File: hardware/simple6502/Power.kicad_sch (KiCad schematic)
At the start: 11 parts, among them J6 AUX 5VDC, U5 74HCT00, U6 74LS30

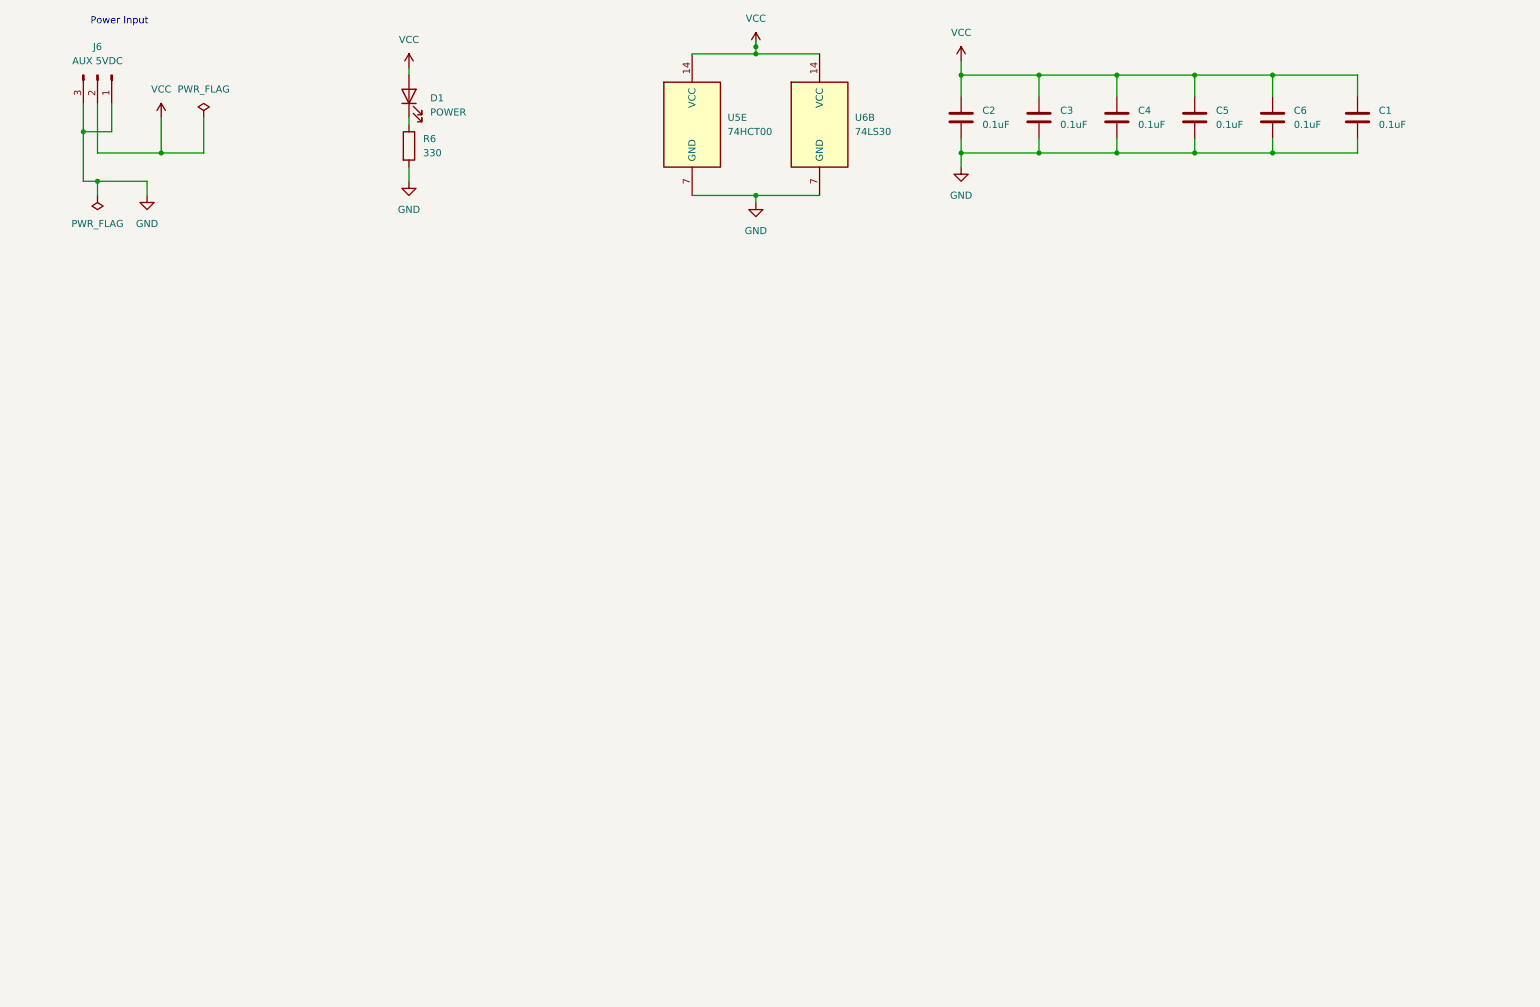
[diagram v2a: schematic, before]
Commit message: Squashed commit of the following:
commit 7c3efda86e123a872d37b7a0967bfebff1f0e87c
Author: Mariano Luna <marianolu@gmail.com>
Date:   Wed Jun 26 21:29:25 2024 -0500

    added license to the read me

commit 04e24ff3751ecfd7aa1644195e6f678569023e69
Author: Mariano Luna <marianolu@gmail.com>
Date:   Wed Jun 26 21:19:54 2024 -0500

    typo fix for {\textunderscore}

commit 2b909ce419fda75b2b3b71af0dca9a0f271ced5f
Author: Mariano Luna <marianolu@gmail.com>
Date:   Wed Jun 26 21:10:17 2024 -0500

    updated ReadME and memory map in the schematic

commit 245ee8cf40a99742bf88408506d7aad409daa5ea
Author: Mariano Luna <marianolu@gmail.com>
Date:   Wed Jun 26 20:32:31 2024 -0500

    minor slikscreen additions

commit ba4f0f790206ee10e8f2da3f956f1fdfcce2d174
Author: Mariano Luna <marianolu@gmail.com>
Date:   Wed Jun 26 20:23:09 2024 -0500

    new PCB pics

commit 7135a14f7811bac113619ea70f1b15383090e088
Author: Mariano Luna <marianolu@gmail.com>
Date:   Wed Jun 26 20:16:23 2024 -0500

    minor silkscreen and trace tidy up

commit cb74d108b563011aa3ae8e77489211a7feb419d9
Author: Mariano Luna <marianolu@gmail.com>
Date:   Wed Jun 26 19:48:35 2024 -0500

    renumer components based on PCB placement

commit 755f9fae4396755bcef755a3da40c138a841726b
Author: Mariano Luna <marianolu@gmail.com>
Date:   Wed Jun 26 19:46:30 2024 -0500

    minor route changes

commit 2a8145687e928c766354ef12103bfb997fda5951
Author: Mariano Luna <marianolu@gmail.com>
Date:   Wed Jun 26 13:28:37 2024 -0500

    port wired, new slot pinout

commit 79f2ca33b26e56ed7b5b5aa909bf5c4120f9fd97
Author: Mariano Luna <marianolu@gmail.com>
Date:   Sat Jun 15 11:24:34 2024 -0500

    add the 40 pin header

commit 10816cce1296760c190b10fc9481db229a365134
Author: Mariano Luna <marianolu@gmail.com>
Date:   Tue Mar 26 20:31:24 2024 -0500

    Updated VCC routing

commit 6f1e481cf970100d714ca12a9d653bae0b6e1127
Author: Mariano Luna <marianolu@gmail.com>
Date:   Tue Mar 26 19:53:34 2024 -0500

    PCB ready DRC passed
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
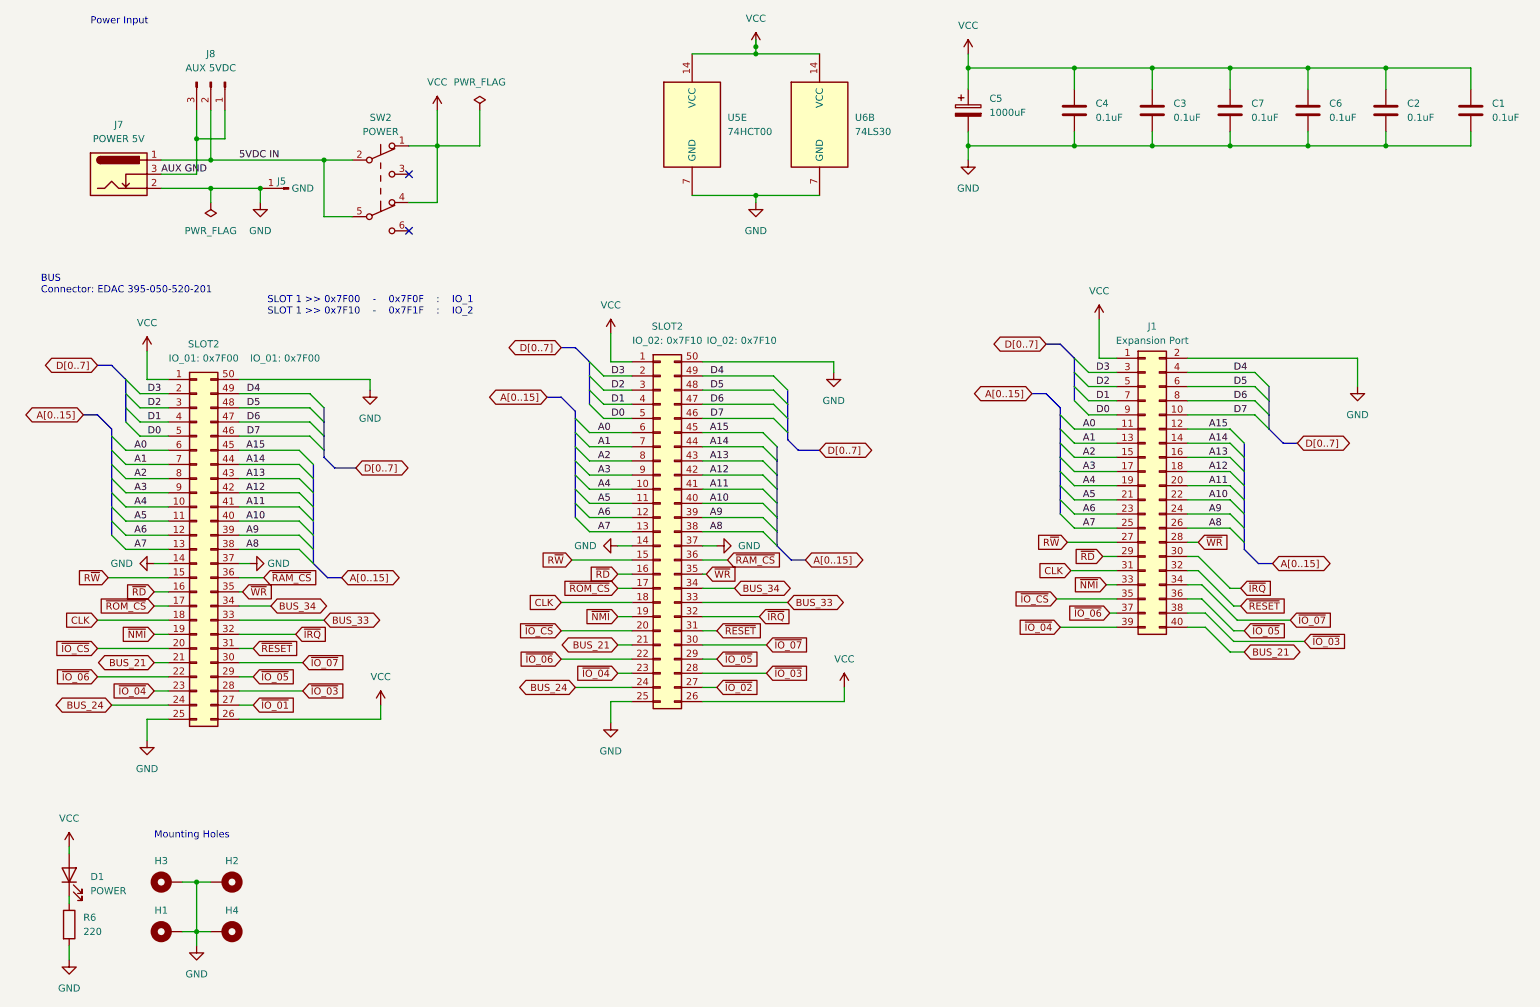
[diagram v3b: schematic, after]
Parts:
- added C5: 1000uF, Capacitor_THT:CP_Radial_D6.3mm_P2.50mm, symbol Device:C_Polarized
- added H1, H2, H3, H4: M, MountingHole:MountingHole_2.7mm_M2.5_Pad_Via, symbol Mechanical:MountingHole_Pad
- added J1: Expansion Port, Connector_PinHeader_2.54mm:PinHeader_2x20_P2.54mm_Vertical, symbol Connector_Generic:Conn_02x20_Odd_Even
- added J5: GND, Connector_PinHeader_2.54mm:PinHeader_1x01_P2.54mm_Vertical, symbol Connector:Conn_01x01_Pin
- added J7: POWER 5V, Connector_BarrelJack:BarrelJack_Horizontal, symbol Connector:Barrel_Jack_Switch
- added SLOT2: IO_02: 0x7F10, Connector_Card:EDAC 395-050-520-201, symbol Connector_Generic:Conn_02x25_Counter_Clockwise
- added SLOT2: IO_01: 0x7F00, Connector_Card:EDAC 395-050-520-201, symbol Connector_Generic:Conn_02x25_Counter_Clockwise
- added SW2: POWER, Button_Switch_THT:SW_Push_2P2T_Toggle_CK_PVA2OAH5xxxxxxV2, symbol Switch:SW_Push_DPDT
- R6: value 330 -> 220
- renumbered C6 to C2, C2 to C4, C5 to C6, C4 to C7, J6 to J8
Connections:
- net GND: now also C5.2, H1.1, H2.1, H3.1, H4.1, J1.2 (Pin_2), J5.1 (Pin_1), J7.2, SLOT2.14 (Pin_14), SLOT2.14 (Pin_14), SLOT2.25 (Pin_25), SLOT2.25 (Pin_25), SLOT2.37 (Pin_37), SLOT2.37 (Pin_37), SLOT2.50 (Pin_50), SLOT2.50 (Pin_50); no longer J8.1 (Pin_1), J8.3 (Pin_3)
- net VCC: now also C5.1, J1.1 (Pin_1), SLOT2.1 (Pin_1), SLOT2.1 (Pin_1), SLOT2.26 (Pin_26), SLOT2.26 (Pin_26), SW2.1 (A), SW2.4 (A); no longer J8.2 (Pin_2)
- new net 5VDC IN: J7.1, J8.2 (Pin_2), SW2.2 (B), SW2.5 (B)
- new net A0: J1.11 (Pin_11), SLOT2.6 (Pin_6), SLOT2.6 (Pin_6)
- new net A1: J1.13 (Pin_13), SLOT2.7 (Pin_7), SLOT2.7 (Pin_7)
- new net A10: J1.22 (Pin_22), SLOT2.40 (Pin_40), SLOT2.40 (Pin_40)
- new net A11: J1.20 (Pin_20), SLOT2.41 (Pin_41), SLOT2.41 (Pin_41)
- new net A12: J1.18 (Pin_18), SLOT2.42 (Pin_42), SLOT2.42 (Pin_42)
- new net A13: J1.16 (Pin_16), SLOT2.43 (Pin_43), SLOT2.43 (Pin_43)
- new net A14: J1.14 (Pin_14), SLOT2.44 (Pin_44), SLOT2.44 (Pin_44)
- new net A15: J1.12 (Pin_12), SLOT2.45 (Pin_45), SLOT2.45 (Pin_45)
- new net A2: J1.15 (Pin_15), SLOT2.8 (Pin_8), SLOT2.8 (Pin_8)
- new net A3: J1.17 (Pin_17), SLOT2.9 (Pin_9), SLOT2.9 (Pin_9)
- new net A4: J1.19 (Pin_19), SLOT2.10 (Pin_10), SLOT2.10 (Pin_10)
- new net A5: J1.21 (Pin_21), SLOT2.11 (Pin_11), SLOT2.11 (Pin_11)
- new net A6: J1.23 (Pin_23), SLOT2.12 (Pin_12), SLOT2.12 (Pin_12)
- new net A7: J1.25 (Pin_25), SLOT2.13 (Pin_13), SLOT2.13 (Pin_13)
- new net A8: J1.26 (Pin_26), SLOT2.38 (Pin_38), SLOT2.38 (Pin_38)
- new net A9: J1.24 (Pin_24), SLOT2.39 (Pin_39), SLOT2.39 (Pin_39)
- new net AUX GND: J7.3, J8.1 (Pin_1), J8.3 (Pin_3)
- new net BUS_21: J1.40 (Pin_40), SLOT2.21 (Pin_21), SLOT2.21 (Pin_21)
- new net BUS_24: SLOT2.24 (Pin_24), SLOT2.24 (Pin_24)
- new net BUS_33: SLOT2.33 (Pin_33), SLOT2.33 (Pin_33)
- new net BUS_34: SLOT2.34 (Pin_34), SLOT2.34 (Pin_34)
- new net CLK: J1.31 (Pin_31), SLOT2.18 (Pin_18), SLOT2.18 (Pin_18)
- new net D0: J1.9 (Pin_9), SLOT2.5 (Pin_5), SLOT2.5 (Pin_5)
- new net D1: J1.7 (Pin_7), SLOT2.4 (Pin_4), SLOT2.4 (Pin_4)
- new net D2: J1.5 (Pin_5), SLOT2.3 (Pin_3), SLOT2.3 (Pin_3)
- new net D3: J1.3 (Pin_3), SLOT2.2 (Pin_2), SLOT2.2 (Pin_2)
- new net D4: J1.4 (Pin_4), SLOT2.49 (Pin_49), SLOT2.49 (Pin_49)
- new net D5: J1.6 (Pin_6), SLOT2.48 (Pin_48), SLOT2.48 (Pin_48)
- new net D6: J1.8 (Pin_8), SLOT2.47 (Pin_47), SLOT2.47 (Pin_47)
- new net D7: J1.10 (Pin_10), SLOT2.46 (Pin_46), SLOT2.46 (Pin_46)
- new net R~{W}: J1.27 (Pin_27), SLOT2.15 (Pin_15), SLOT2.15 (Pin_15)
- new net ~{IO_01}: SLOT2.27 (Pin_27)
- new net ~{IO_02}: SLOT2.27 (Pin_27)
- new net ~{IO_03}: J1.38 (Pin_38), SLOT2.28 (Pin_28), SLOT2.28 (Pin_28)
- new net ~{IO_04}: J1.39 (Pin_39), SLOT2.23 (Pin_23), SLOT2.23 (Pin_23)
- new net ~{IO_05}: J1.36 (Pin_36), SLOT2.29 (Pin_29), SLOT2.29 (Pin_29)
- new net ~{IO_06}: J1.37 (Pin_37), SLOT2.22 (Pin_22), SLOT2.22 (Pin_22)
- new net ~{IO_07}: J1.34 (Pin_34), SLOT2.30 (Pin_30), SLOT2.30 (Pin_30)
- new net ~{IO_CS}: J1.35 (Pin_35), SLOT2.20 (Pin_20), SLOT2.20 (Pin_20)
- new net ~{IRQ}: J1.30 (Pin_30), SLOT2.32 (Pin_32), SLOT2.32 (Pin_32)
- new net ~{NMI}: J1.33 (Pin_33), SLOT2.19 (Pin_19), SLOT2.19 (Pin_19)
- new net ~{RAM_CS}: SLOT2.36 (Pin_36), SLOT2.36 (Pin_36)
- new net ~{RD}: J1.29 (Pin_29), SLOT2.16 (Pin_16), SLOT2.16 (Pin_16)
- new net ~{RESET}: J1.32 (Pin_32), SLOT2.31 (Pin_31), SLOT2.31 (Pin_31)
- new net ~{ROM_CS}: SLOT2.17 (Pin_17), SLOT2.17 (Pin_17)
- new net ~{WR}: J1.28 (Pin_28), SLOT2.35 (Pin_35), SLOT2.35 (Pin_35)
- no-connect marks 0 -> 2
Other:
- note added: "BUS Connector: EDAC 395-050-520-201"
- note added: "Mounting Holes"
- note added: "SLOT 1 >> 0x7F00 - 0x7F0F : IO_1 SLOT 1 >> 0x7F10 - 0x7F1F : IO_2"
- title: simple6502 -> All in One - simple6502
- moved on the sheet: C1, C2, C3, C4, C6, C7, D1, J8, R6

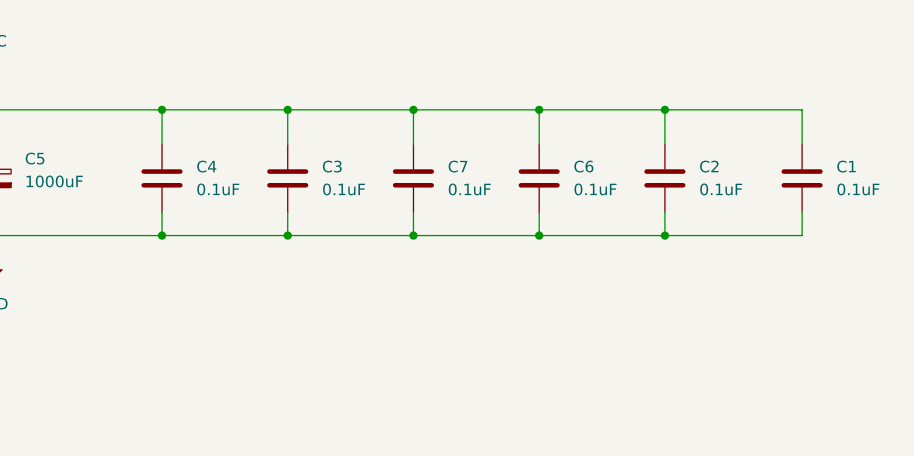
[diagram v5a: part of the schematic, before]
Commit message: Revision 1.6.1 Moved C5 and added C8
Moved C5 to make space for a slim ZIF for the ROM.
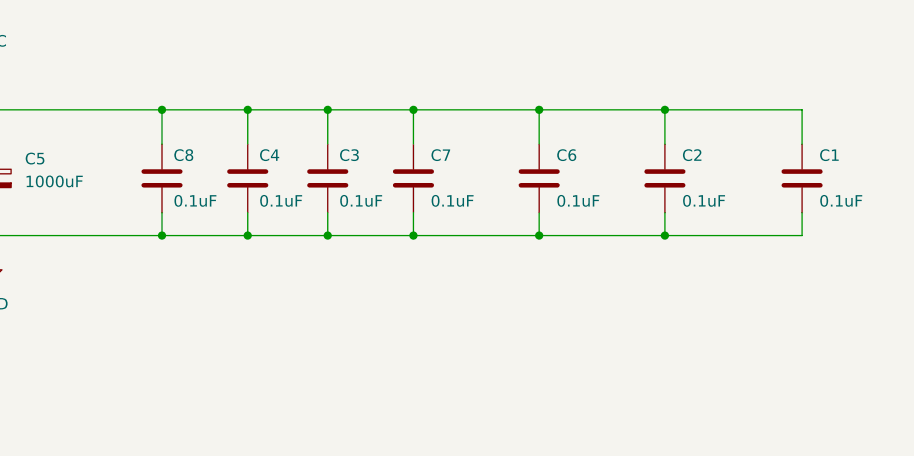
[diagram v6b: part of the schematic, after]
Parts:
- added C8: 0.1uF, Capacitor_THT:C_Disc_D3.0mm_W1.6mm_P2.50mm, symbol Device:C
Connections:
- net GND: now also C8.2
- net VCC: now also C8.1
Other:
- moved on the sheet: C3, C4

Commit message: PCB Rev 1.7 - rewire FTDI
using a more standard pinout for the FTDI header
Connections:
- net 5VDC IN renamed 5V_IN
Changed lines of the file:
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@@
     (title "All in One - simple6502")
     (date "2024-06-26")
-    (rev "1.6.1")
+    (rev "1.7")
     (company "Mariano Luna")
   )
@@
   )
   (junction (at 257.81 29.21) (diameter 0) (color 0 0 0 0)
+  )
+  (junction (at 59.055 45.72) (diameter 0) (color 0 0 0 0)
   )
   (junction (at 46.99 45.72) (diameter 0) (color 0 0 0 0)
@@
     (stroke (width 0) (type default))
   )
-  (wire (pts (xy 46.99 45.72) (xy 67.31 45.72))
+  (wire (pts (xy 46.99 45.72) (xy 59.055 45.72))
     (stroke (width 0) (type default))
   )
@@
     (stroke (width 0) (type default))
   )
+  (wire (pts (xy 59.055 45.72) (xy 67.31 45.72))
+    (stroke (width 0) (type default))
+  )
   (wire (pts (xy 67.31 45.72) (xy 67.31 55.88))
     (stroke (width 0) (type default))
@@
   )
   (wire (pts (xy 222.25 119.38) (xy 224.155 119.38))
+    (stroke (width 0) (type default))
+  )
+  (wire (pts (xy 59.055 41.275) (xy 59.055 45.72))
     (stroke (width 0) (type default))
   )
@@
     (effects (font (size 1.27 1.27)) (justify right bottom))
   )
-  (label "5VDC IN" (at 52.07 45.72 0) (fields_autoplaced)
-    (effects (font (size 1.27 1.27)) (justify left bottom))
-  )
   (label "A4" (at 205.74 104.14 180) (fields_autoplaced)
     (effects (font (size 1.27 1.27)) (justify right bottom))
@@
     )
   )
+  (global_label "5V_IN" (shape input) (at 59.055 41.275 90) (fields_autoplaced)
+    (effects (font (size 1.27 1.27)) (justify left))
+    (property "Intersheetrefs" "${INTERSHEET_REFS}" (at 59.055 33.0888 90)
+      (effects (font (size 1.27 1.27)) (justify left) hide)
+    )
+  )
